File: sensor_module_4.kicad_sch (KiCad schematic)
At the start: 46 parts, among them J1 Conn_Coaxial, J15 SLOT 1, J3 Conn_Coaxial, J4 Conn_Coaxial, J5 Conn_Coaxial, U12 REF3025, U13 MCP3204, U16 INA333xxDGK, U17 INA333xxDGK, U18 INA333xxDGK, U5 OPA1678, U6 M24C02-WMN, U7 TPS22929D, U8 REF3040

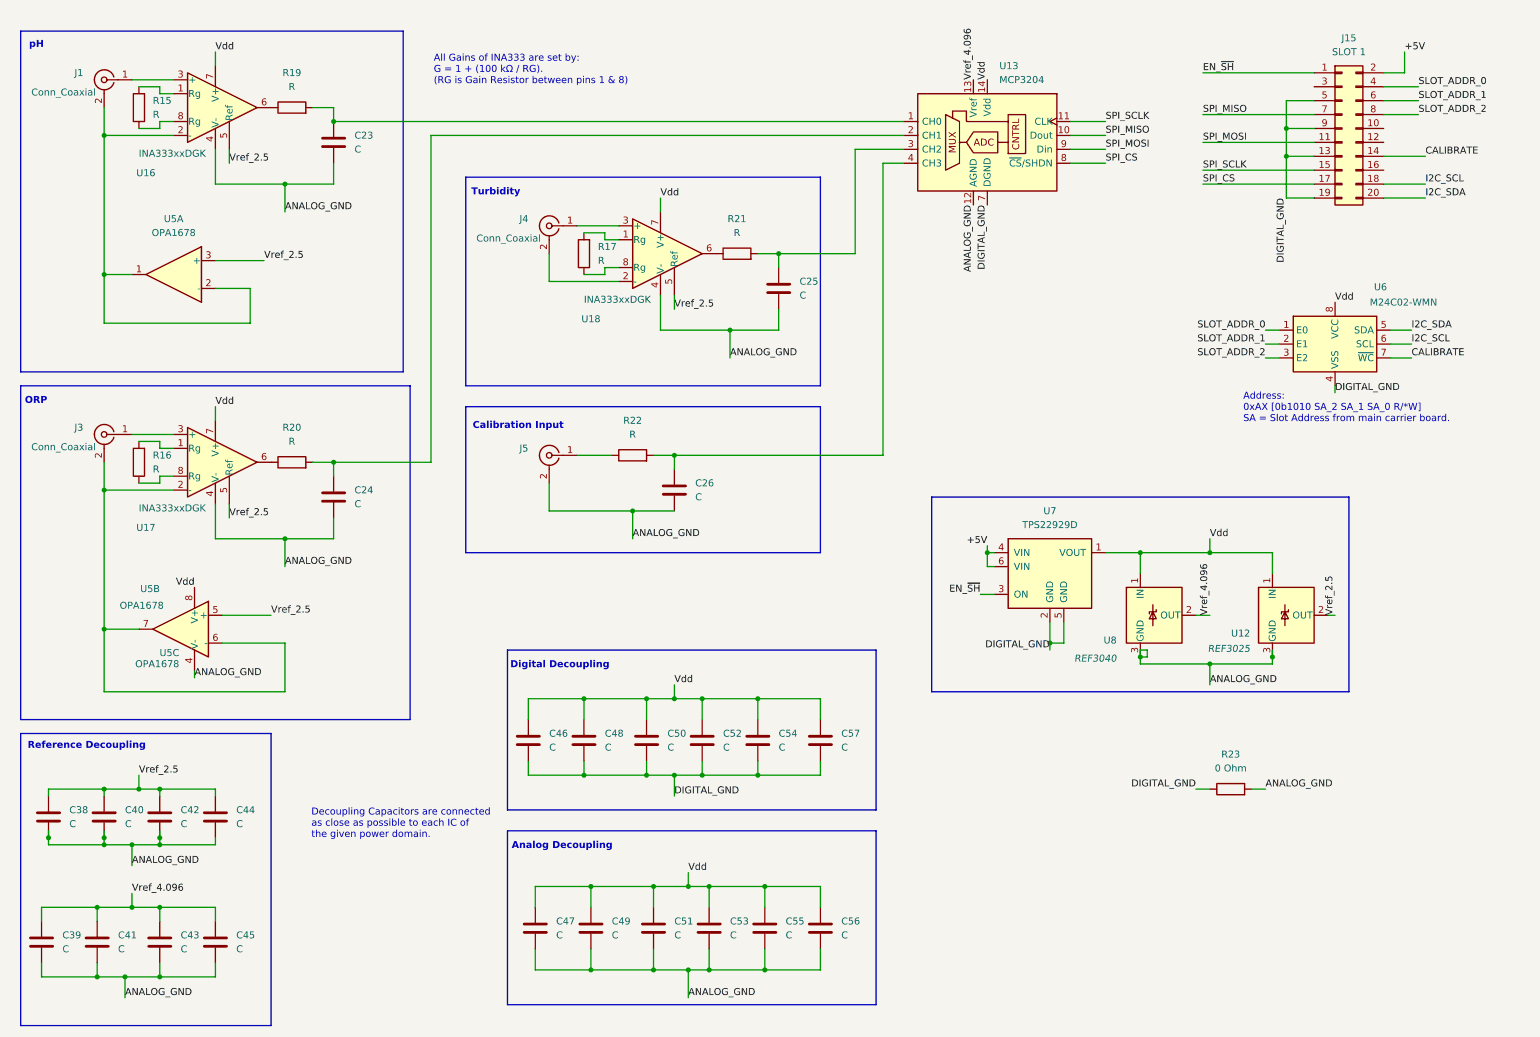
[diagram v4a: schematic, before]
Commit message: Updated the ORP and pH probes with a more appropriate amp. Added some notes. Added a tentative PL-100 adapter circuit. Added Vref buffering. Started move towards ESP32 ADC converter for base sensors.
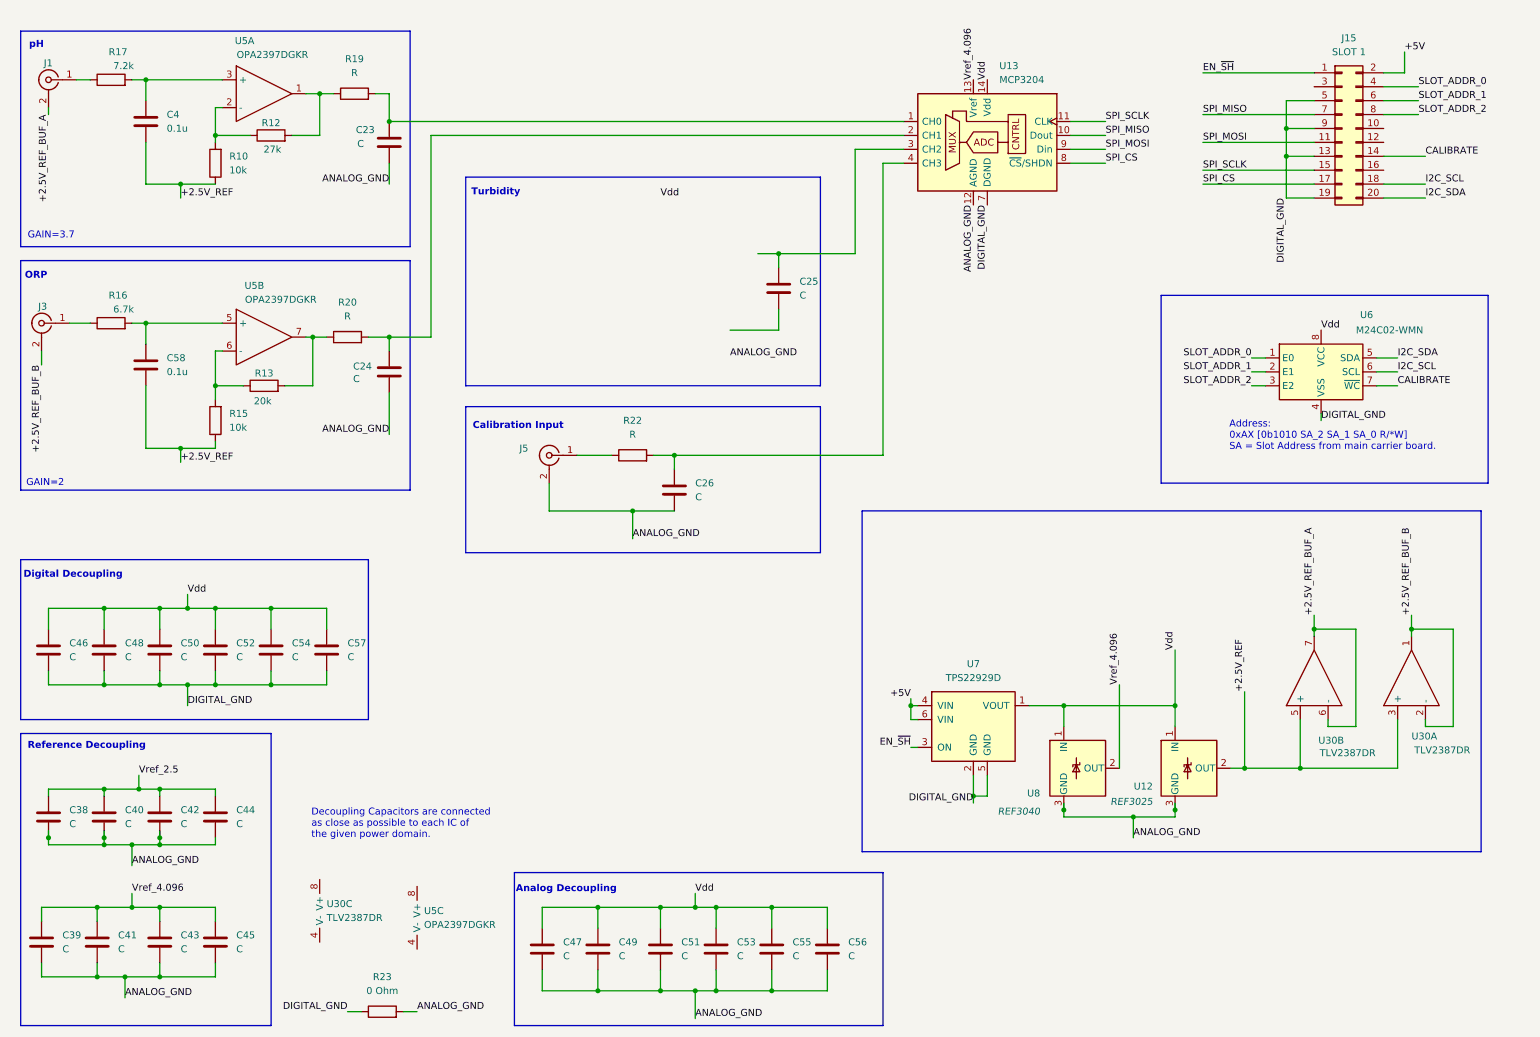
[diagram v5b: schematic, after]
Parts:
- removed J4: Conn_Coaxial, symbol Connector:Conn_Coaxial
- removed R21: R, symbol Device:R
- removed U16, U17, U18: INA333xxDGK, Package_SO:VSSOP-8_3x3mm_P0.65mm, symbol Amplifier_Instrumentation:INA333xxDGK
- removed U5: OPA1678, symbol Amplifier_Operational:OPA1678
- added C4, C58: 0.1u, symbol Device:C
- added R10: 10k, symbol Device:R
- added R12: 27k, symbol Device:R
- added R13: 20k, symbol Device:R
- added U30: TLV2387DR, Package_SO:SOIC-8_3.9x4.9mm_P1.27mm, symbol Op-Amp-Extended:TLV2387DR
- added U5: OPA2397DGKR, Package_SO:SOIC-8_3.9x4.9mm_P1.27mm, symbol Op-Amp-Extended:OPA2397DR
- R15: value R -> 10k
- R16: value R -> 6.7k
- R17: value R -> 7.2k
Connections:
- net ANALOG_GND: no longer C25.2
- net Vref_2.5: no longer U12.2 (OUT)
- net at R16.1: now also J3.1 (In)
- net at R16.2: now also C58.1, U5.5 (+)
- net at R19.1: now also R12.2, U5.1
- net +2.5V_REF_BUF_A: now reaches J1.2 (Ext)
- net +2.5V_REF_BUF_A: now also U30.6 (-), U30.7
- net at R17.2: now also C4.1, U5.3 (+)
- net at R17.1: now also J1.1 (In)
- net +2.5V_REF: now reaches R15.1
- net +2.5V_REF: now also U12.2 (OUT), C4.2, C58.2, R10.1, U30.3 (+), U30.5 (+)
- net at R15.2: now also R13.1, U5.6 (-)
- net +2.5V_REF_BUF_B: now reaches J3.2 (Ext)
- net +2.5V_REF_BUF_B: now also U30.1, U30.2 (-)
- net at R20.1: now also R13.2, U5.7
- new net: R10.2, R12.1, U5.2 (-)
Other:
- note added: "GAIN=2"
- note added: "GAIN=3.7"
- note removed: "All Gains of INA333 are set by: G = 1 + (100 kΩ / RG). (RG is Gain Resistor between pins 1 & 8)"
- moved on the sheet: C23, C24, C46, C47, C48, C49, C50, C51, C52, C53, C54, C55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

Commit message: More notes and comments Cleaned up some signal lines Compacted the decoupling sections Added Turbidity placeholder
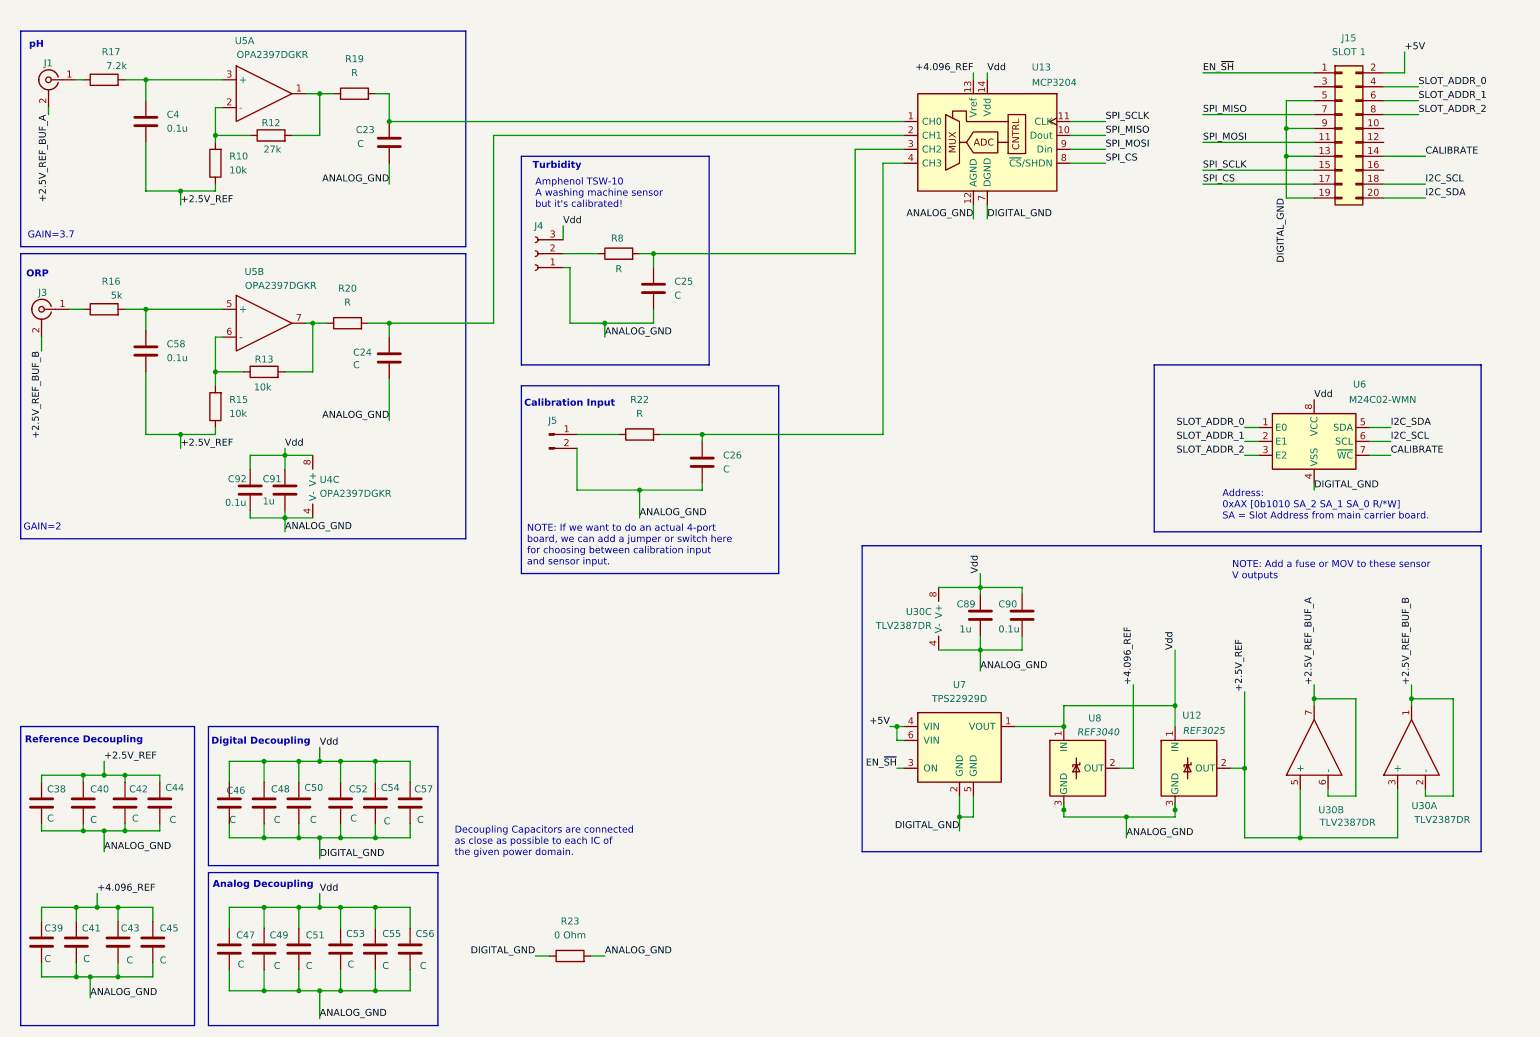
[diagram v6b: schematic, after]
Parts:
- removed J5: Conn_Coaxial, symbol Connector:Conn_Coaxial
- removed unit 3 of U5
- added C89, C91: 1u, symbol Device:C
- added C90, C92: 0.1u, symbol Device:C
- added J4: Conn_01x03_Socket, symbol Connector:Conn_01x03_Socket
- added J5: Conn_01x02_Pin, symbol Connector:Conn_01x02_Pin
- added R8: R, symbol Device:R
- added U4: OPA2397DGKR, Package_SO:SOIC-8_3.9x4.9mm_P1.27mm, symbol Op-Amp-Extended:OPA2397DR
- R13: value 20k -> 10k
- R16: value 6.7k -> 5k
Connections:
- net Vref_2.5 is gone; now on net +2.5V_REF: C38.1, C40.1, C42.1, C44.1
- net ANALOG_GND: now also C25.2, U30.4 (V-), C89.2, C90.2, C91.2, C92.2, J4.1 (Pin_1), J5.2 (Pin_2), U4.4 (V-)
- net Vdd: now also U30.8 (V+), C89.1, C90.1, C91.1, C92.1, J4.3 (Pin_3), U4.8 (V+)
- net at R22.1: now also J5.1 (Pin_1)
- net at C25.1, U13.3 (CH2): now also R8.2
- net Vref_4.096 renamed +4.096_REF
- new net: J4.2 (Pin_2), R8.1
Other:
- note added: "Amphenol TSW-10 A washing machine sensor but it's calibrated!"
- note added: "NOTE: Add a fuse or MOV to these sensor V outputs"
- note added: "NOTE: If we want to do an actual 4-port board, we can add a jumper or switch here for choosing between calibration input and sensor input."
- moved on the sheet: C24, C25, C26, C38, C40, C41, C42, C43, C44, C45, C46, C47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

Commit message: Cleaned up a bit Added a SPDT to calibrate signal on the base board Added PTC and MOV to power section
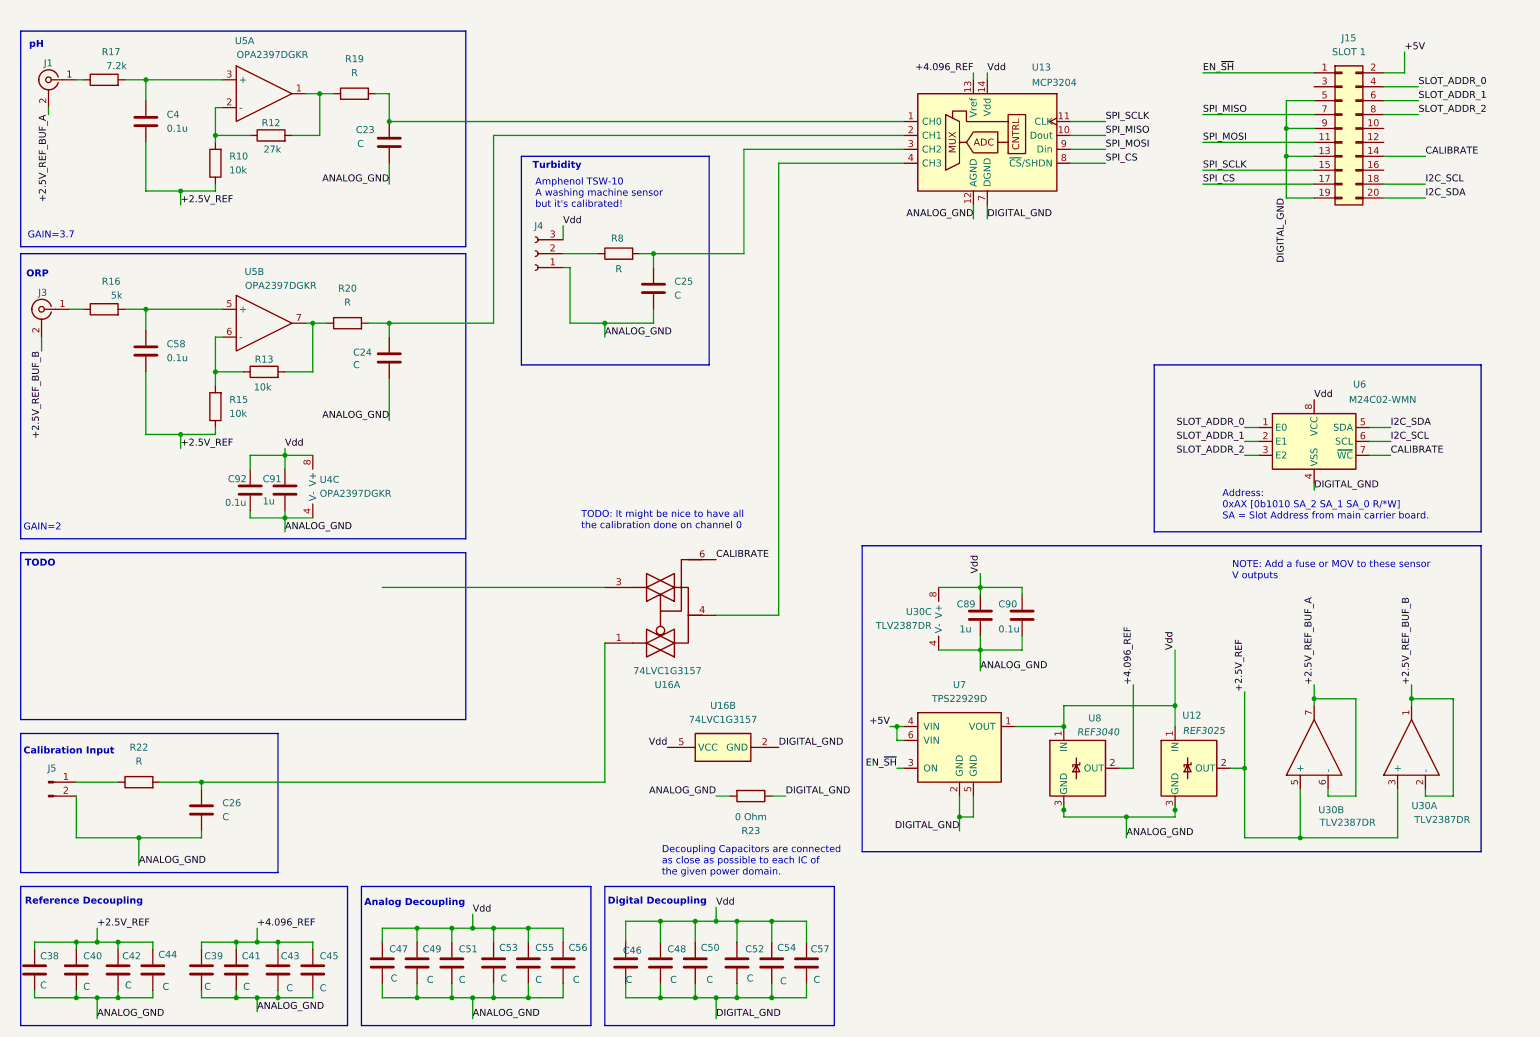
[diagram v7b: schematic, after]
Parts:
- added U16: 74LVC1G3157, symbol 74xGxx:74LVC1G3157
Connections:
- net CALIBRATE: now also U16.6
- net DIGITAL_GND: now also U16.2 (GND)
- net Vdd: now also U16.5 (VCC)
- net at C26.1, R22.2: now also U16.1; no longer U13.4 (CH3)
- new net: U13.4 (CH3), U16.4
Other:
- note added: "TODO"
- note added: "TODO: It might be nice to have all the calibration done on channel 0"
- note removed: "NOTE: If we want to do an actual 4-port board, we can add a jumper or switch here for choosing between calibration input and sensor input."
- moved on the sheet: C26, C38, C39, C40, C41, C42, C43, C44, C45, C46, C47, C48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
